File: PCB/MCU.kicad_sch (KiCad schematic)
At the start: 38 parts, among them J1 SWD, J2 TC2030-NL, J3 VIK Keyboard Expansion, J4 OLED Breakout, SW1 PTS645, SW2 PTS645, U1 ZD25WQ32CEIGR, U2 RP2040, U3 SN74AHCT1G125, U4 REF3033, Y1 12MHz

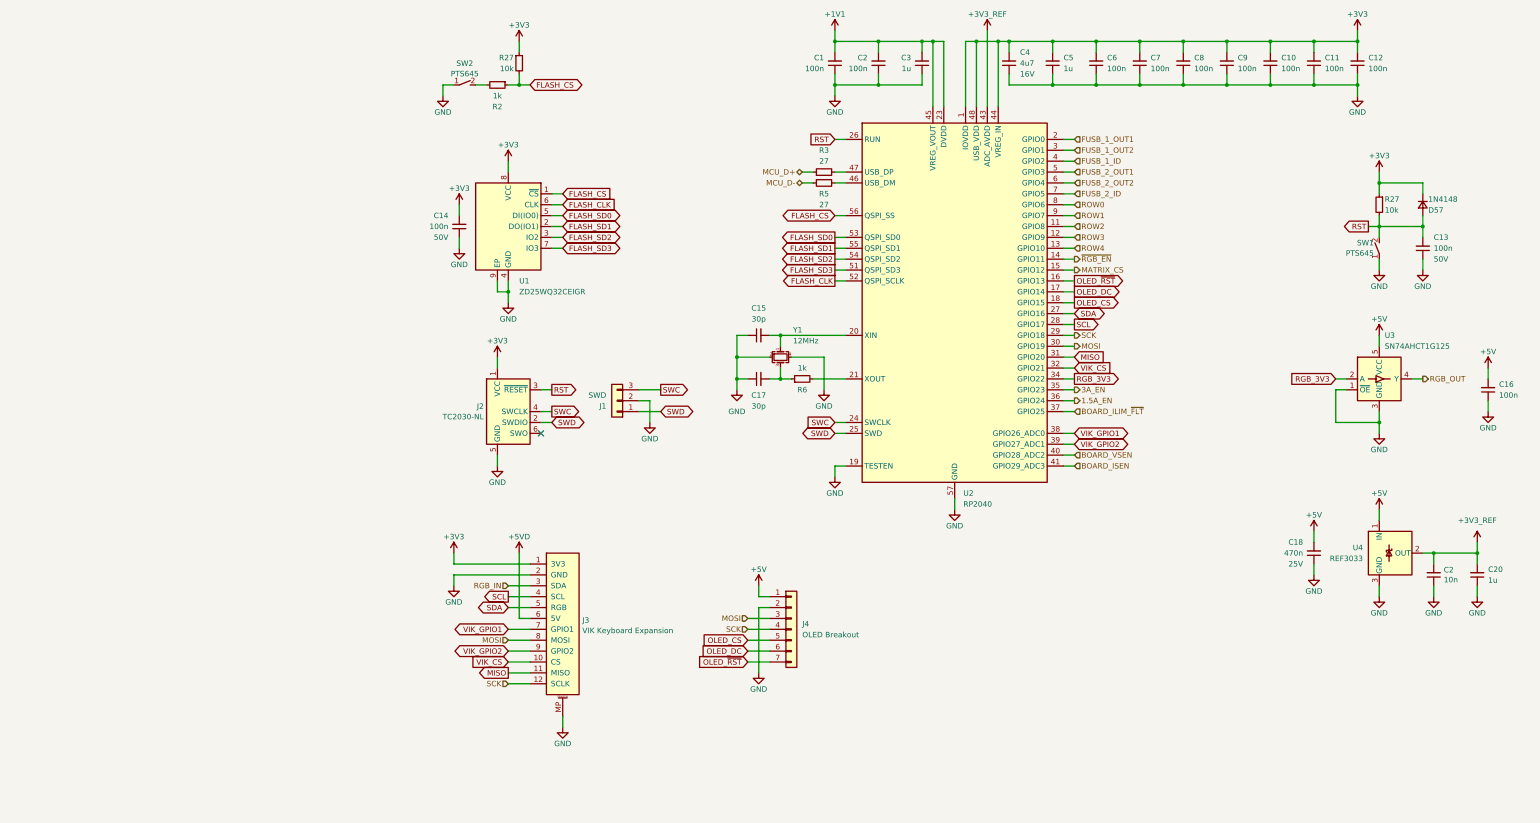
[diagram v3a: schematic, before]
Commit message: 23/08/2023 update
Changed MCU to nRF52840. Added nPM1300 PMIC for power management. Replaced SSD1351 display with Nice!View. Added Kailh Choc V1/V2 and Gateron KS-27/KS-33 support.
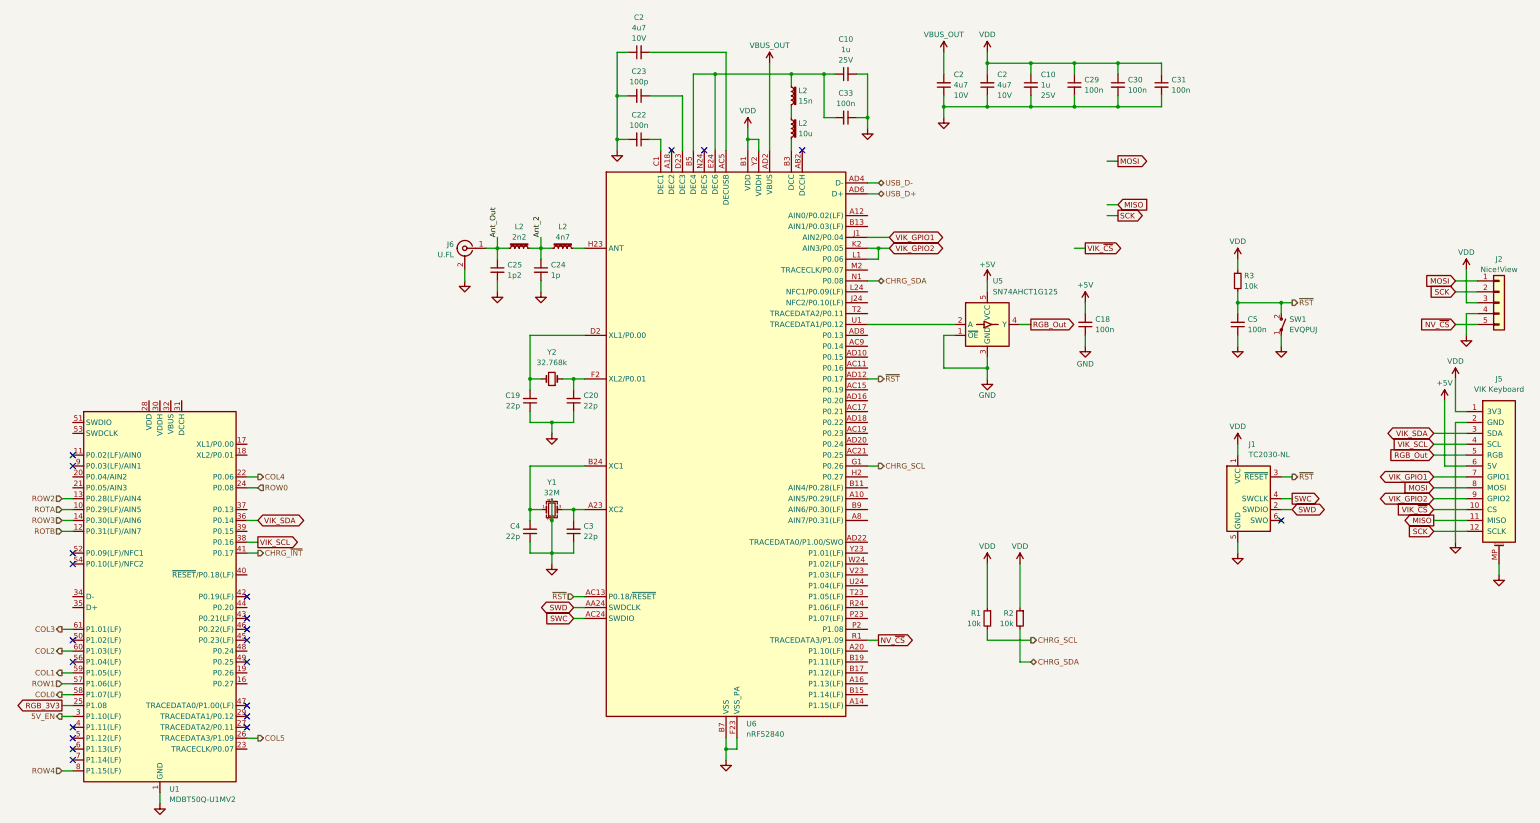
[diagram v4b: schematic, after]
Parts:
- removed C1, C10, C11, C12, C14, C16, C2, C6, C7, C8, C9: 100n, Capacitor_SMD:C_0402_1005Metric, symbol Device:C_Small
- removed C15, C17: 30p, Capacitor_SMD:C_0402_1005Metric, symbol Device:C_Small
- removed C2: 10n, Capacitor_SMD:C_0402_1005Metric, symbol Device:C_Small
- removed C5: 1u, Capacitor_SMD:C_0402_1005Metric, symbol Device:C_Small
- removed D57: 1N4148, Cantaloupe:D_SOD-323, symbol Device:D_Small
- removed J1: SWD, Cantaloupe:Header_SWD, symbol Connector_Generic:Conn_01x03
- removed J3: VIK Keyboard Expansion, Cantaloupe:vik-keyboard-connector-horizontal, symbol Honeydew:vik-keyboard-connector
- removed J4: OLED Breakout, Cantaloupe:OLED_1.5_SSD1351_128x128, symbol Connector_Generic:Conn_01x07
- removed R27 (x2): 10k, Resistor_SMD:R_0402_1005Metric, symbol Device:R_Small
- removed R5: 27, Resistor_SMD:R_0402_1005Metric, symbol Device:R_Small
- removed R6: 1k, Resistor_SMD:R_0402_1005Metric, symbol Device:R_Small
- removed SW1, SW2: PTS645, Cantaloupe:SW_SPST_PTS645, symbol Cantaloupe:SW_SPST_Small
- removed U1: ZD25WQ32CEIGR, Cantaloupe:USON-8-1EP_3x2mm_P0.5mm_EP1.6x0.2mm, symbol Memory_Flash:W25Q32JVZP
- removed U2: RP2040, Cantaloupe:QFN-56-1EP_7x7mm_P0.4mm_EP3.2x3.2mm_ThermalVias, symbol MCU_RaspberryPi:RP2040
- removed U3: SN74AHCT1G125, Package_TO_SOT_SMD:SOT-353_SC-70-5, symbol Honeydew:SN74AHCT1G125
- removed U4: REF3033, Cantaloupe:SOT-23-3, symbol Reference_Voltage:REF3033
- added C10 (x2): 1u, Ariamelon-Device:C_0402_1005Metric, symbol Device:C_Small
- added C19: 22p, Ariamelon-Device:C_0402_1005Metric, symbol Device:C_Small
- added C2 (x3): 4u7, Ariamelon-Device:C_0402_1005Metric, symbol Device:C_Small
- added C22, C29, C30, C31, C33: 100n, Ariamelon-Device:C_0402_1005Metric, symbol Device:C_Small
- added C23: 100p, Ariamelon-Device:C_0402_1005Metric, symbol Device:C_Small
- added C24: 1p, Ariamelon-Device:C_0402_1005Metric, symbol Device:C_Small
- added C25: 1p2, Ariamelon-Device:C_0402_1005Metric, symbol Device:C_Small
- added J2: Nice!View, Ariamelon-Breakout:Breakout_Nice!View_Flippable, symbol Connector_Generic:Conn_01x05
- added J5: VIK Keyboard, Ariamelon-Connector:VIK_Keyboard_Horizontal, symbol Ariamelon-Connector:VIK Keyboard Connector
- added J6: U.FL, Connector_Coaxial:U.FL_Hirose_U.FL-R-SMT-1_Vertical, symbol Connector:Conn_Coaxial
- added L2: 4n7, Ariamelon-Device:L_0402_1005Metric, symbol Device:L_Iron_Small
- added L2: 15n, Ariamelon-Device:L_0402_1005Metric, symbol Device:L_Iron_Small
- added L2: 2n2, Ariamelon-Device:L_0402_1005Metric, symbol Device:L_Iron_Small
- added L2: 10u, Ariamelon-Device:L_0603_1608Metric, symbol Device:L_Iron_Small
- added R1: 10k, Ariamelon-Device:R_0402_1005Metric, symbol Device:R_Small
- added SW1: EVQPUJ, Ariamelon-Switch:SW_Panasonic_EVQPUL_EVQPUC, symbol Ariamelon-Switch:SW_SPST_Small
- added U1: MDBT50Q-U1MV2, Ariamelon-Breakout:Breakout_Raytac_MDBT50Q-U1MV2, symbol Ariamelon-MCU:MDBT50Q-U1MV2
- added U5: SN74AHCT1G125, Package_TO_SOT_SMD:SOT-353_SC-70-5, symbol Ariamelon-IC:SN74AHCT1G125
- added U6: nRF52840, Ariamelon-Package:Nordic_AQFN-73-1EP_7x7mm_P0.5mm, symbol Ariamelon-IC:nRF52840
- added Y2: 32.768k, Ariamelon-Device:Crystal_SMD_2012-2Pin_2.0x1.2mm, symbol Device:Crystal_Small
- C18: value 470n -> 100n; footprint Capacitor_SMD:C_0603_1608Metric -> Ariamelon-Device:C_0402_1005Metric; LCSC C1623 -> C307331; Voltage 25V -> 50V
- C20, C3: value 1u -> 22p; footprint Capacitor_SMD:C_0402_1005Metric -> Ariamelon-Device:C_0402_1005Metric; LCSC C52923 -> C1555; Voltage 25V -> 50V
- C4: value 4u7 -> 22p; footprint Capacitor_SMD:C_0603_1608Metric -> Ariamelon-Device:C_0402_1005Metric; LCSC C19666 -> C1555; Voltage 16V -> 50V
- C5: renamed from C13; footprint Capacitor_SMD:C_0402_1005Metric -> Ariamelon-Device:C_0402_1005Metric
- R2: value 1k -> 10k; footprint Resistor_SMD:R_0402_1005Metric -> Ariamelon-Device:R_0402_1005Metric; LCSC C11702 -> C25744
- R3: value 27 -> 10k; footprint Resistor_SMD:R_0402_1005Metric -> Ariamelon-Device:R_0402_1005Metric; LCSC C25100 -> C25744
- Y1: value 12MHz -> 32M; footprint Crystal:Crystal_SMD_3225-4Pin_3.2x2.5mm -> Ariamelon-Device:Crystal_SMD_2016-4Pin_2.0x1.6mm; LCSC C9002 -> C255896
- renumbered J2 to J1
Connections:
- net +1V1 is gone; now on an unnamed net: C3.2
- net FLASH_CS is gone; now on net VDD: R2.1
- net MCU_D+ is gone; now on net VDD: R3.1
- net RST is gone; now on net ~{RST}: C5.2, J1.3 (~{RESET})
- net +5V: now also J5.6 (5V), U5.5 (VCC)
- net GND: now also C10.2, C10.2, C19.1, C2.1, C2.1, C2.1, C22.2, C23.2, C24.2, C25.2, C29.2, C30.2, C31.2, C33.1, J2.4 (Pin_4), J5.2 (GND), J5.MP, J6.2 (Ext), SW1.1 (A), U1.1 (GND), U1.15 (GND), U1.2 (GND), U1.33 (GND), U1.55 (GND), U5.1 (~{OE}), U5.3 (GND), U6.B7 (VSS), U6.EP (VSS), U6.F23 (VSS_PA)
- net MISO: now also J5.11 (MISO)
- net MOSI: now also J2.1 (Pin_1), J5.8 (MOSI)
- net RGB_3V3: now also U1.25 (P1.08)
- net ROW0: now also U1.24 (P0.08)
- net ROW1: now also U1.57 (P1.06(LF))
- net ROW2: now also U1.13 (P0.28(LF)/AIN4)
- net ROW3: now also U1.14 (P0.30(LF)/AIN6)
- net ROW4: now also U1.8 (P1.15(LF))
- net SCK: now also J2.2 (Pin_2), J5.12 (SCLK)
- net SWC: now also U6.AC24 (SWDIO)
- net SWD: now also U6.AA24 (SWDCLK)
- net VIK_GPIO1: now also J5.7 (GPIO1), U6.J1 (AIN2/P0.04)
- net VIK_GPIO2: now also J5.9 (GPIO2), U6.K2 (AIN3/P0.05), U6.L1 (P0.06)
- net at Y1.3: now also U6.A23 (XC2)
- net at Y1.1: now also C4.2, U6.B24 (XC1)
- net ~{RST}: now reaches R3.2
- net ~{RST}: now also SW1.2 (B), U6.AC13 (P0.18/~{RESET}), U6.AD12 (P0.17)
- net CHRG_SDA: now reaches R2.2
- net CHRG_SDA: now also U6.N1 (P0.08)
- net +3V3 renamed VDD
- net VDD: now also C10.1, C2.2, C29.1, C30.1, C31.1, J2.3 (Pin_3), J5.1 (3V3), R1.1, U6.A22 (VDD), U6.AD14 (VDD), U6.AD23 (VDD), U6.B1 (VDD), U6.W1 (VDD), U6.Y2 (VDDH); no longer C4.2
- net +3V3_REF: no longer names the net of C20.2
- net +3V3_REF: now also U6.F2 (XL2/P0.01), Y2.1
- new net: C2.2, U6.AC5 (DECUSB)
- new net: L2.1, U6.B3 (DCC)
- new net: C10.1, C33.2, L2.2, U6.B5 (DEC4), U6.E24 (DEC6)
- new net: C22.1, U6.C1 (DEC1)
- new net: C19.2, U6.D2 (XL1/P0.00), Y2.2
- new net: C23.1, U6.D23 (DEC3)
- new net: L2.1, U6.H23 (ANT)
- new net: U5.2 (A), U6.U1 (TRACEDATA1/P0.12)
- new net: L2.1, L2.2
- new net 5V_EN: U1.3 (P1.10(LF))
- new net Ant_2: C24.1, L2.1, L2.2
- new net Ant_Out: C25.1, J6.1 (In), L2.2
- new net CHRG_SCL: R1.2, U6.G1 (P0.26)
- new net CHRG_~{INT}: U1.41 (P0.17)
- new net COL0: U1.58 (P1.07(LF))
- new net COL1: U1.59 (P1.05(LF))
- new net COL2: U1.60 (P1.03(LF))
- new net COL3: U1.61 (P1.01(LF))
- new net COL4: U1.22 (P0.06)
- new net COL5: U1.26 (TRACEDATA3/P1.09)
- new net NV_~{CS}: J2.5 (Pin_5), U6.R1 (TRACEDATA3/P1.09)
- new net RGB_Out: J5.5 (RGB), U5.4 (Y)
- new net ROTA: U1.10 (P0.29(LF)/AIN5)
- new net ROTB: U1.12 (P0.31(LF)/AIN7)
- new net USB_D+: U6.AD6 (D+)
- new net USB_D-: U6.AD4 (D-)
- new net VBUS_OUT: C2.2, U6.AD2 (VBUS)
- new net VIK_SCL: J5.4 (SCL), U1.38 (P0.16)
- new net VIK_SDA: J5.3 (SDA), U1.36 (P0.14)
- new net VIK_~{CS}: J5.10 (CS)
- no-connect marks 1 -> 22
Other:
- moved on the sheet: C5, J1

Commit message: 24/08/2023 update
Finished routing. Consolidated all libraries into Ariamelon's Kicad Master Library. Added PCM12 switch connected to nPM1300 GPIO. Rearranged components and rerouted.
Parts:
- removed U1: MDBT50Q-U1MV2, Ariamelon-Breakout:Breakout_Raytac_MDBT50Q-U1MV2, symbol Ariamelon-MCU:MDBT50Q-U1MV2
- J6: footprint Connector_Coaxial:U.FL_Hirose_U.FL-R-SMT-1_Vertical -> Ariamelon-Connector:U.FL_Hirose_U.FL-R-SMT-1_Vertical
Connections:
- net VIK_SCL is gone; now on net SCL: J5.4 (SCL)
- net VIK_SDA is gone; now on net SDA: J5.3 (SDA)
- net CHRG_~{INT}: now also U6.G1 (P0.26)
- net COL0: now also J1.6 (SWO), U6.AD22 (TRACEDATA0/P1.00/SWO)
- net COL1: now also U6.AC21 (P0.25)
- net COL2: now also U6.W24 (P1.02(LF))
- net COL3: now also U6.U24 (P1.04(LF))
- net COL4: now also U6.R24 (P1.06(LF))
- net COL5: now also U6.J24 (NFC2/P0.10(LF))
- net MISO: now also U6.AD18 (P0.22)
- net MOSI: now also U6.AD10 (P0.15)
- net NV_~{CS}: now also U6.AD8 (P0.13); no longer U6.R1 (TRACEDATA3/P1.09)
- net ROTA: now also U6.A10 (AIN5/P0.29(LF))
- net ROTB: now also U6.A12 (AIN0/P0.02(LF))
- net ROW0: now also U6.L24 (NFC1/P0.09(LF))
- net ROW1: now also U6.A20 (P1.10(LF))
- net ROW2: now also U6.A16 (P1.13(LF))
- net ROW3: now also U6.A14 (P1.15(LF))
- net ROW4: now also U6.A8 (AIN7/P0.31(LF))
- net SCK: now also U6.AD20 (P0.24)
- net VIK_~{CS}: now also U6.AD16 (P0.20)
- net CHRG_SCL renamed SCL
- net SCL: now also U6.N1 (P0.08); no longer U6.G1 (P0.26)
- net CHRG_SDA renamed SDA
- net SDA: now also U6.R1 (TRACEDATA3/P1.09); no longer U6.N1 (P0.08)
- no-connect marks 22 -> 3
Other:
- moved on the sheet: R1, R2, U5

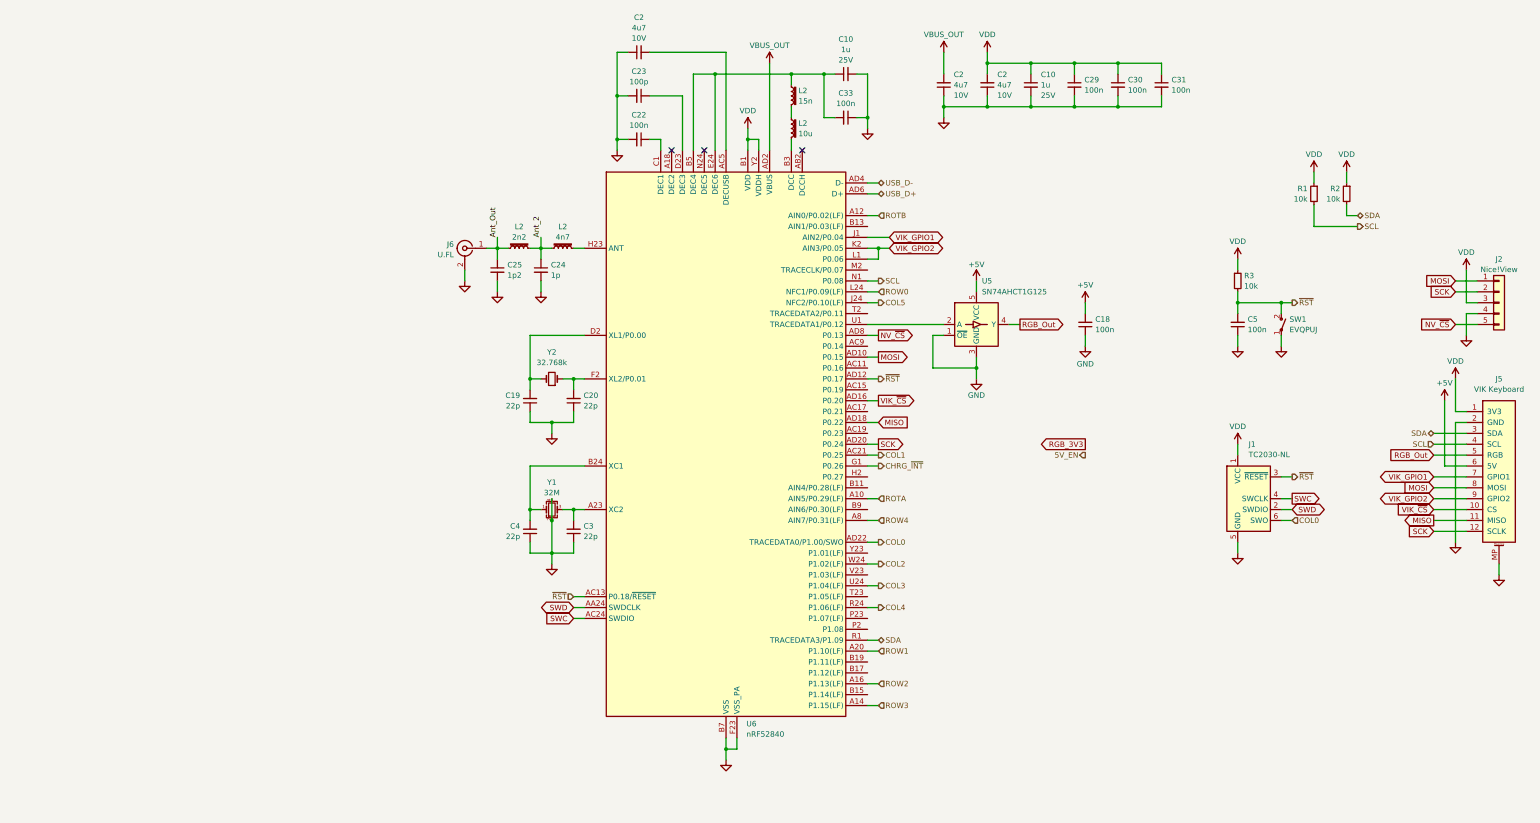
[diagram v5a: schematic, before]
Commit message: Cantaloupe V3.0 name changed to CantaloupeBT V1.0 ('BT-V1' branch). Key features updated. Design will be reworked in the coming days!
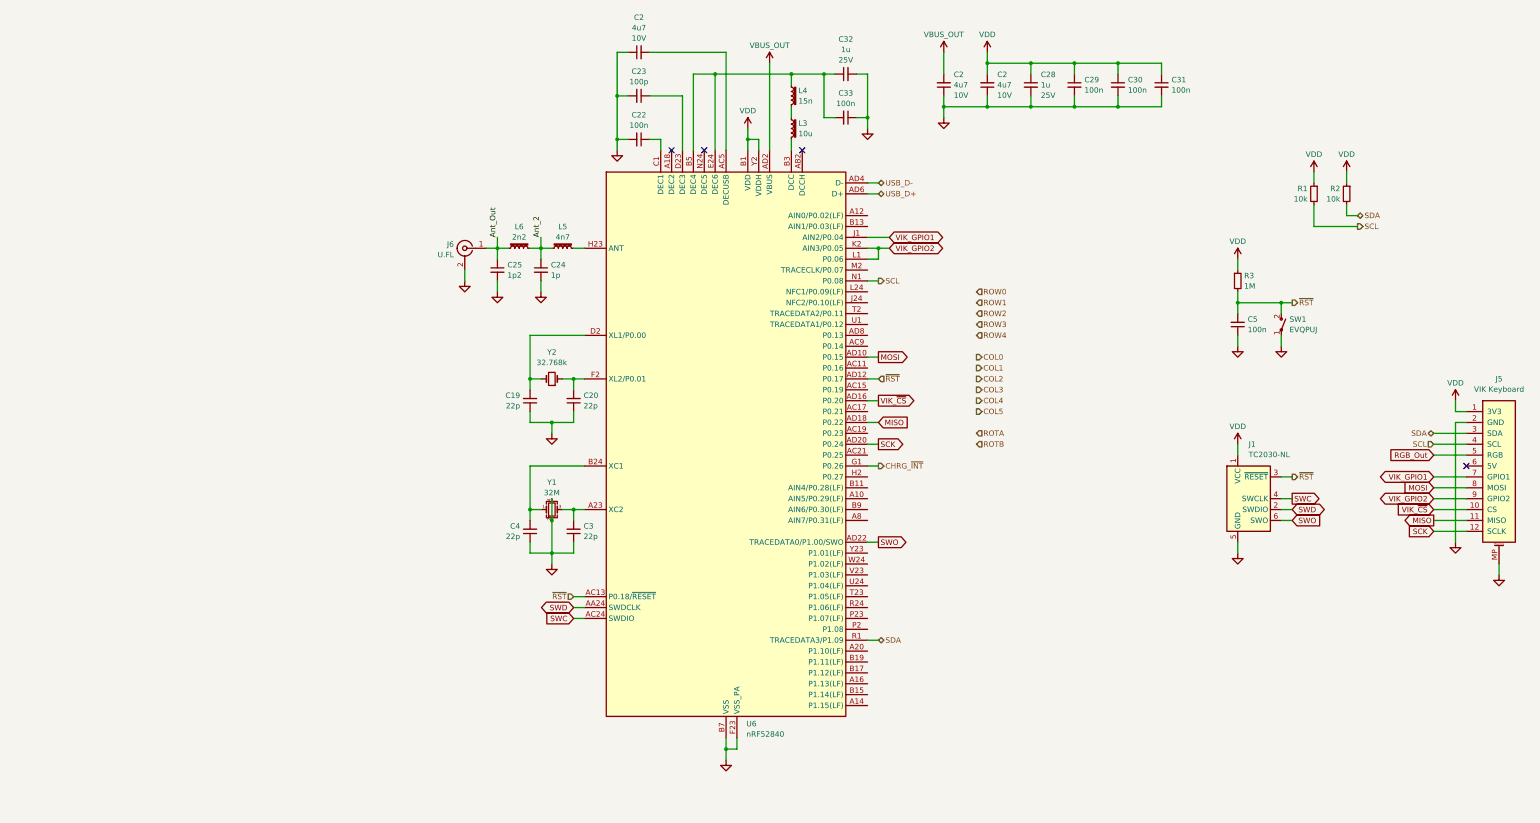
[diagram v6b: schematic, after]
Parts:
- removed C18: 100n, Ariamelon-Device:C_0402_1005Metric, symbol Device:C_Small
- removed J2: Nice!View, Ariamelon-Breakout:Breakout_Nice!View_Flippable, symbol Connector_Generic:Conn_01x05
- removed U5: SN74AHCT1G125, Package_TO_SOT_SMD:SOT-353_SC-70-5, symbol Ariamelon-IC:SN74AHCT1G125
- R3: value 10k -> 1M; LCSC C25744 -> C26083
- renumbered C10 to C28, C10 to C32, L2 to L3, L2 to L4, L2 to L5, L2 to L6
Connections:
- net COL0: no longer J1.6 (SWO), U6.AD22 (TRACEDATA0/P1.00/SWO)
- net COL1: no longer U6.AC21 (P0.25)
- net COL2: no longer U6.W24 (P1.02(LF))
- net COL3: no longer U6.U24 (P1.04(LF))
- net COL4: no longer U6.R24 (P1.06(LF))
- net COL5: no longer U6.J24 (NFC2/P0.10(LF))
- net ROTA: no longer U6.A10 (AIN5/P0.29(LF))
- net ROTB: no longer U6.A12 (AIN0/P0.02(LF))
- net ROW0: no longer U6.L24 (NFC1/P0.09(LF))
- net ROW1: no longer U6.A20 (P1.10(LF))
- net ROW2: no longer U6.A16 (P1.13(LF))
- net ROW3: no longer U6.A14 (P1.15(LF))
- net ROW4: no longer U6.A8 (AIN7/P0.31(LF))
- net +5V: no longer names the net of J5.6 (5V)
- net NV_~{CS}: no longer names the net of U6.AD8 (P0.13)
- new net SWO: J1.6 (SWO), U6.AD22 (TRACEDATA0/P1.00/SWO)
- no-connect marks 3 -> 4
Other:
- title: Cantaloupe split ergonomic keyboard -> CantaloupeLP split ergonomic keyboard
